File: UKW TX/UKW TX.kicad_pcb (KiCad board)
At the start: 2 copper layers, 59 x 31 mm, 39 parts, among them P1 CONN_01X01, P2 CONN_01X01, P3 CONN_01X05, T1 TRANSFO, U1 AP1117D33, U2 THS9001, U3 Alps_603A, Y1 32,768kHz

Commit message: platine fertig.
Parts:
- added CON1: BARREL_JACK, lpis2812:LUM1503, F.Cu at (127.0, 100.5)
- moved T1 18.0 mm to (156.0, 104.0)
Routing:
- net /Ton_L: track 0.00 -> 42.2 mm, vias 0 -> 1
- net /Ton_R: track 0.00 -> 26.6 mm, vias 0 -> 1
- net Net-(P1-Pad1): track 13.5 -> 34.8 mm
- net Net-(P2-Pad1): track 12.6 -> 32.0 mm
- net Net-(C4-Pad1): track 28.2 -> 9.94 mm
- net GND: track 42.8 -> 42.3 mm
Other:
- board size 59 x 31 mm -> 38.5 x 27 mm
- board text added: "Design verfügbar auf GitHub https://github.com/Virtex7/Kefersender Philipp Hörauf - 2015"

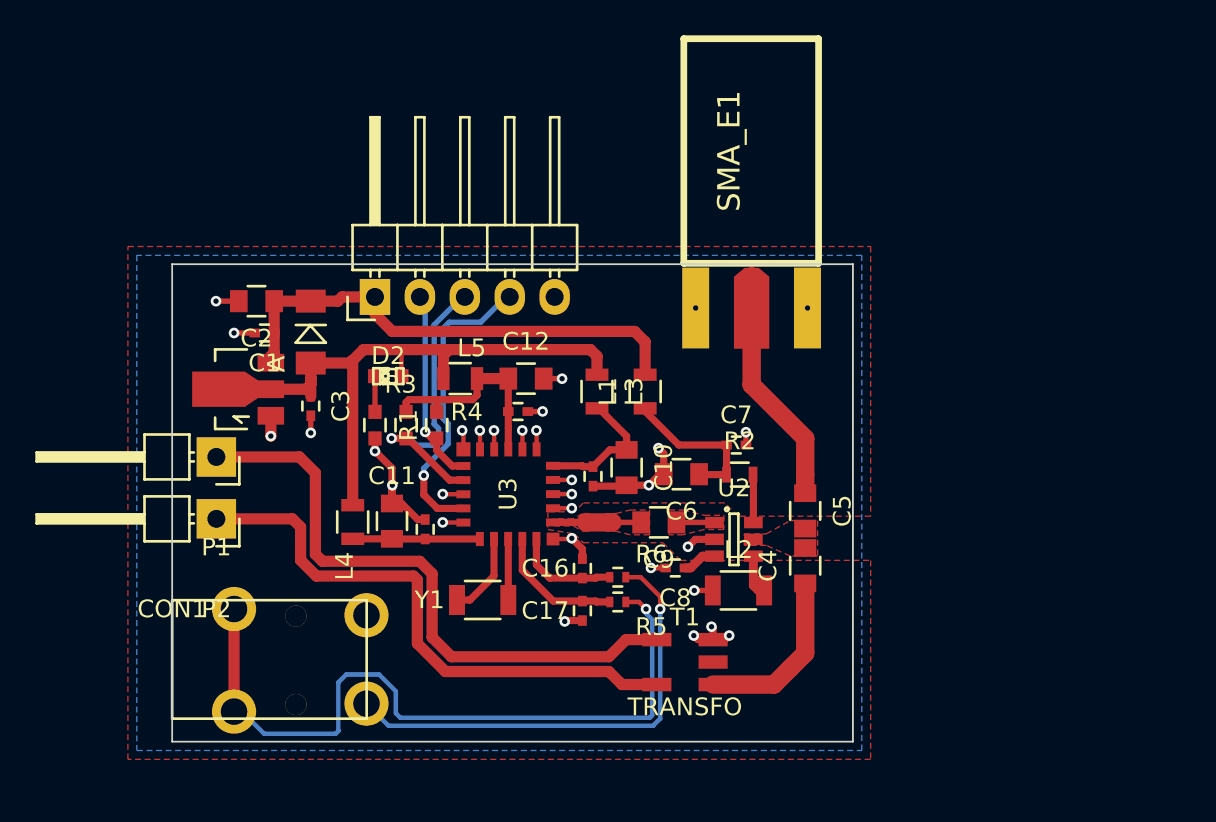
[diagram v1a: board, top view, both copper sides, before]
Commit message: platine fertig - incl anpassleitung
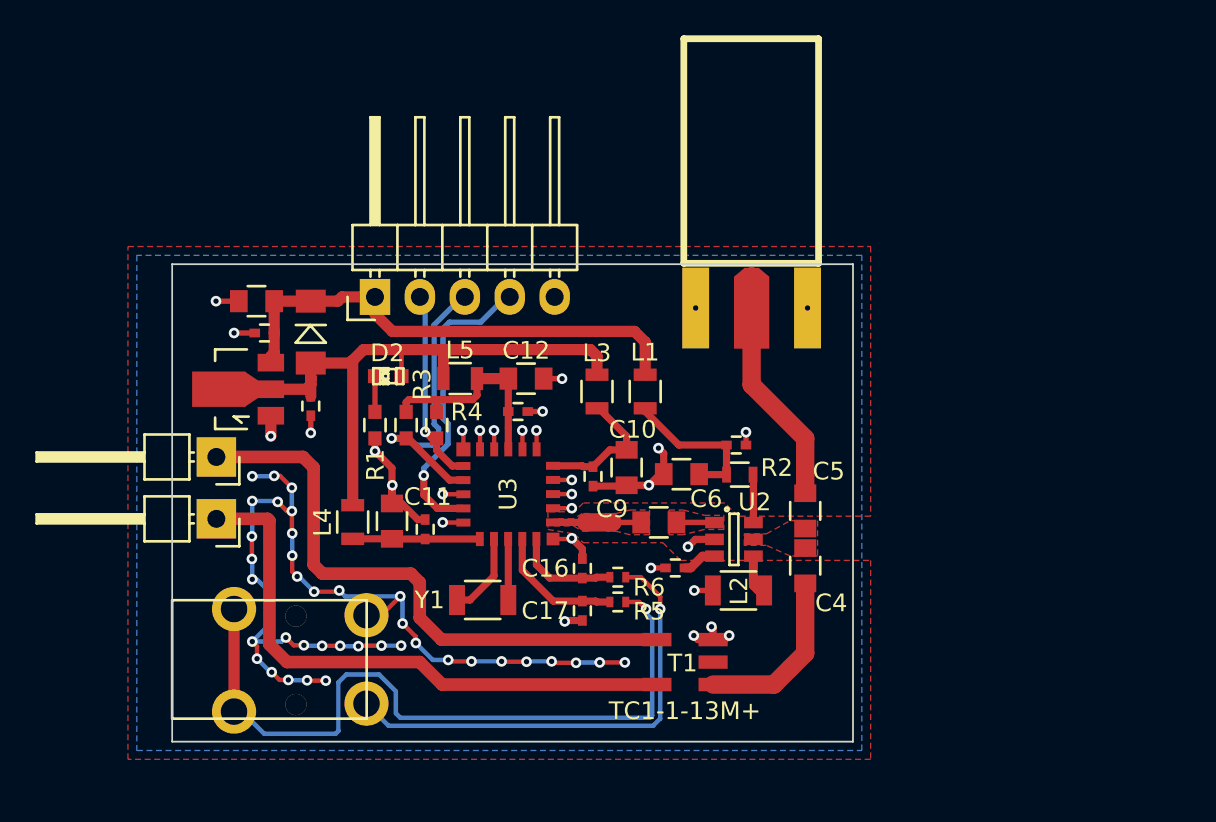
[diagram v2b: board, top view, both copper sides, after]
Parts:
- CON1: value BARREL_JACK -> LUM1503
- T1: value TRANSFO -> TC1-1-13M+
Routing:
- net GND: track 42.3 -> 99.6 mm, vias 31 -> 69
- net Net-(P1-Pad1): track 34.8 -> 33.6 mm
- net Net-(P2-Pad1): track 32.0 -> 32.9 mm
